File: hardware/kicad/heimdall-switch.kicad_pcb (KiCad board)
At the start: 2 copper layers, 53 x 23 mm, 42 parts, among them J1 SWD (ARM 10-pin), J2 LOAD_OUT, J3 BATT_IN, J4 B3B-XH-A, Q1 AO3400A, Q2 BSS84, Q3 AO4407A, Q4 AO4407A, Q5 AO3400A, Q6 BSS84, SW1 PTS810, U1 BT832, U2 TPS629206, Y1 32.768kHz

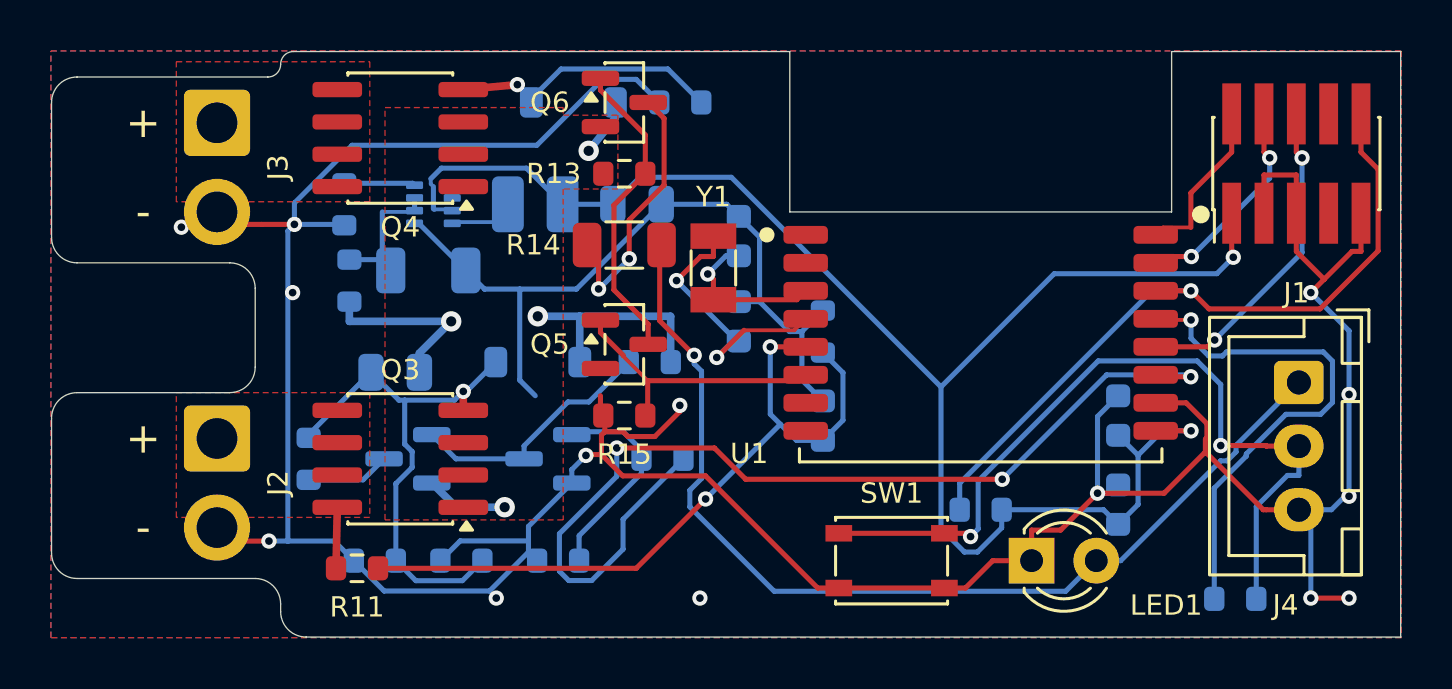
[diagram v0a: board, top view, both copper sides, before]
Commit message: Main PCB: BAT/OUT on silk instead of the J3/J2 references
The labels sit right of each wire pair, outside the heat shrink. The
J3/J2 references move to the fab layer.

Co-Authored-By: Claude Opus 5.5 <noreply@anthropic.com>
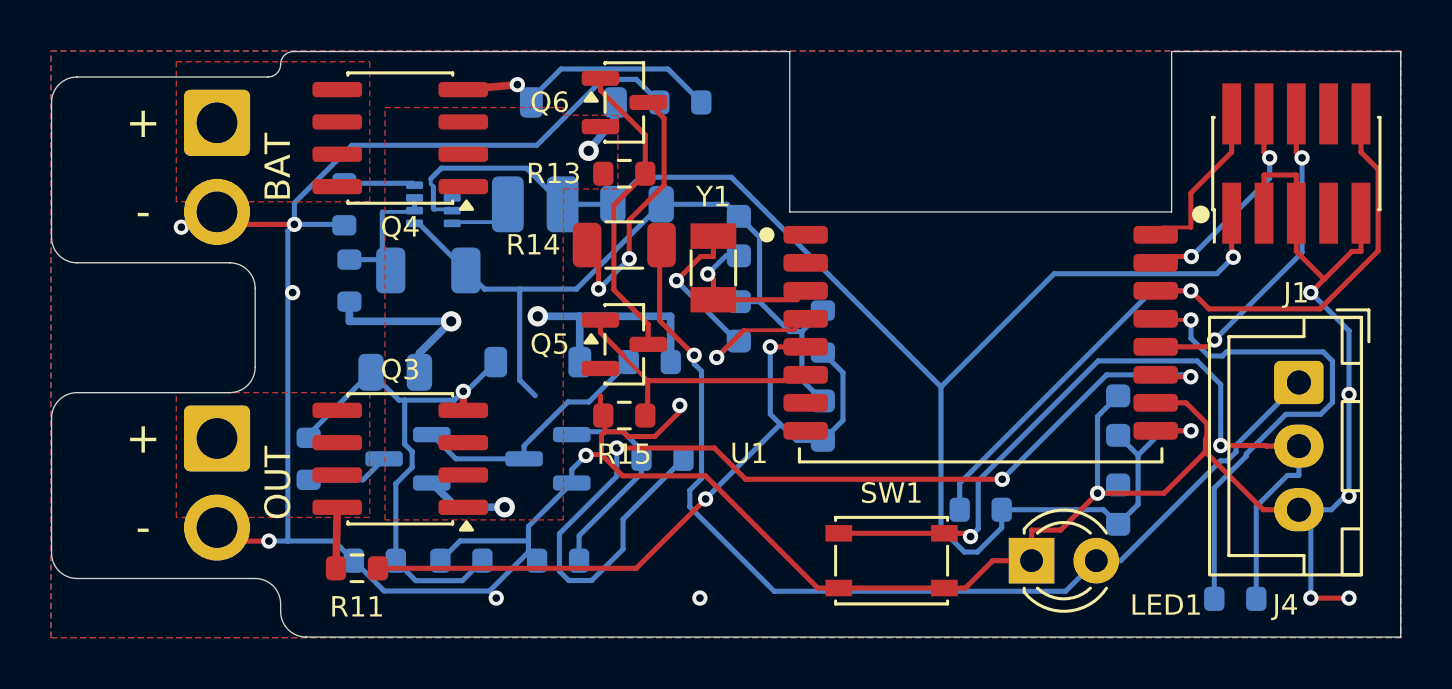
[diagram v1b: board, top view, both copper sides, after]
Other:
- board text added: "BAT"
- board text added: "OUT"
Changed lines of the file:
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@@
 		(tags "connector wire 0.75sqmm")
 		(property "Reference" "J3"
-			(at 1.75 -2.4 90)
-			(layer "F.SilkS")
+			(at 1.75 0 0)
+			(layer "F.Fab")
 			(effects
 				(font
@@
 		(tags "connector wire 0.75sqmm")
 		(property "Reference" "J2"
-			(at 1.75 -2.4 90)
-			(layer "F.SilkS")
+			(at 1.75 0 0)
+			(layer "F.Fab")
 			(effects
 				(font
@@
 		(layer "Edge.Cuts")
 	)
+	(gr_text "BAT"
+		(at 104.9 104.55 90)
+		(layer "F.SilkS")
+		(effects
+			(font
+				(size 1 1)
+				(thickness 0.15)
+			)
+		)
+	)
+	(gr_text "OUT"
+		(at 104.9 116.95 90)
+		(layer "F.SilkS")
+		(effects
+			(font
+				(size 1 1)
+				(thickness 0.15)
+			)
+		)
+	)
 	(gr_text "+"

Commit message: Main PCB: solid B.Cu GND strap for the load return
The OUT- to BAT- return had to squeeze past R8 around the slot end
(~1mm of B.Cu). Now a no-tracks rule area keeps a GND strap free:
3.5mm on B past OUT+, >=2.4mm on B plus ~4.3mm F.Cu beside the slot
end, with a 6-via block where the F copper hands down to the strap.
R8 moved below Q2, R9/R10 shifted down; re-routed, U2-EN finished by
hand. 49 vias, ~570mm. DRC clean, full parity.

Co-Authored-By: Claude Opus 5.5 <noreply@anthropic.com>
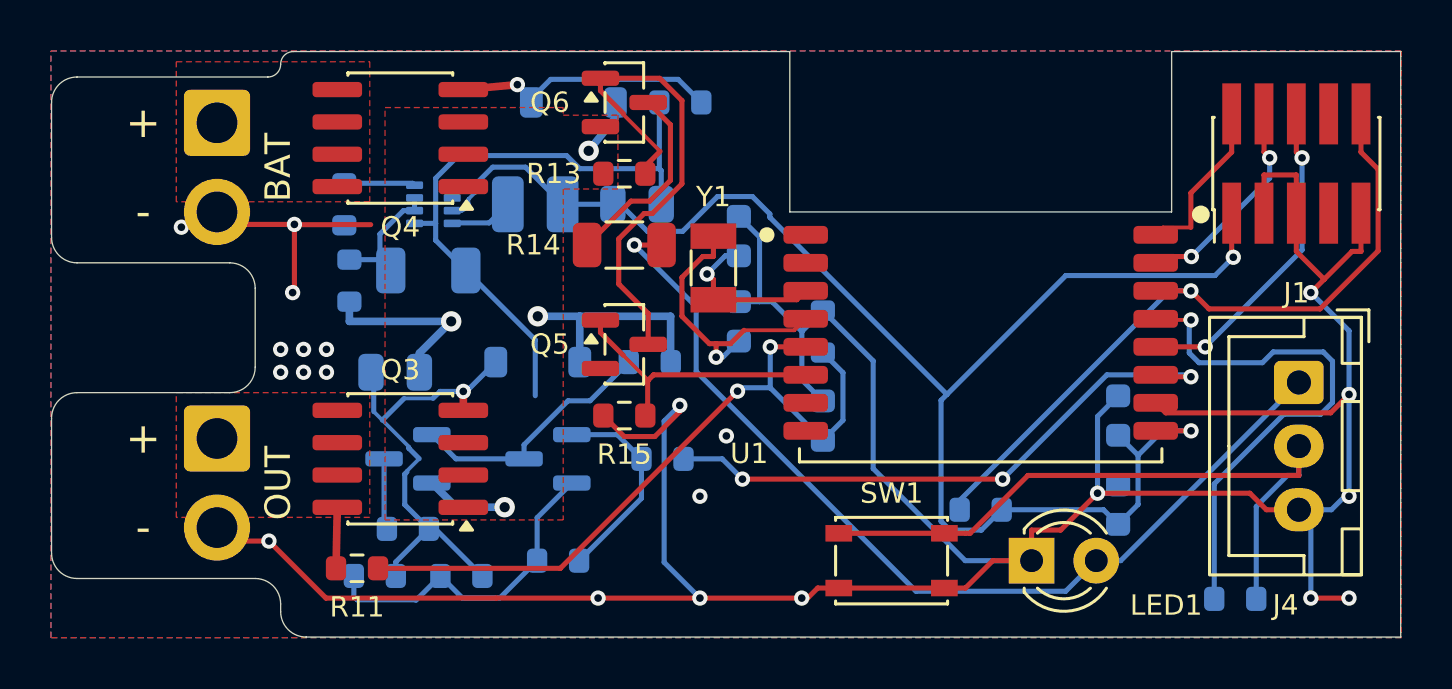
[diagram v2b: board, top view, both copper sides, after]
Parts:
- moved R8 4.77 mm to (110.0, 118.8), turned to 0 degrees
- moved R10 0.60 mm to (112.1, 120.6)
- moved R9 0.60 mm to (108.7, 120.6)
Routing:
- net /OUT_OFF: track 39.7 -> 23.4 mm
- net Net-(Q5-D): track 12.2 -> 19.8 mm
- net GND: track 164.9 -> 171.3 mm, vias 14 -> 22
- net Net-(J4-Pin_2): track 31.8 -> 27.1 mm, vias 2 -> 0
- net +3V3: track 64.3 -> 61.4 mm
- net Net-(Q6-D): track 10.6 -> 7.75 mm, vias 2 -> 0
- net /LED_A: track 40.0 -> 37.7 mm
- net /Q3_GATE: track 21.1 -> 19.0 mm
- net /BTN: track 20.3 -> 21.0 mm
- net Net-(Q2-D): track 3.30 -> 2.80 mm
- net Net-(U1-P0.01_XL2): track 11.2 -> 11.3 mm, vias 2 -> 1

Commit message: Main PCB: tidy GND vias at the wire pads
BAT- island: the scattered vias become a 2 x 5 grid (1.2mm pitch, ~10A
layer transfer). Dropped the redundant via beside the BAT- pad on the
tab, the leftover via and stub at OUT-, and the autorouter's GND stubs
into both pads (the plated pads join the pours directly). DRC clean.

Co-Authored-By: Claude Opus 5.5 <noreply@anthropic.com>
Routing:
- net GND: track 171.3 -> 157.0 mm
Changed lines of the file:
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@@
-	)
-	(segment
-		(start 105.47 109.47)
-		(end 105.54 109.4)
-		(width 0.2)
-		(layer "F.Cu")
-		(net "GND")
 	)
 	(segment
@@
 	)
 	(segment
-		(start 104.54 119.23)
-		(end 106.78 121.47)
-		(width 0.2)
-		(layer "F.Cu")
-		(net "GND")
-	)
-	(segment
-		(start 104.54 119.23)
-		(end 103.03 119.23)
-		(width 0.2)
-		(layer "F.Cu")
-		(net "GND")
-	)
-	(segment
 		(start 145.47 109.47)
 		(end 145.9942 108.9458)
@@
 	)
 	(segment
-		(start 108.5379 106.7995)
-		(end 105.5495 106.7995)
-		(width 0.2)
-		(layer "F.Cu")
-		(net "GND")
-	)
-	(segment
 		(start 131.075 121.075)
 		(end 131.9017 121.075)
@@
 	)
 	(segment
-		(start 105.54 109.4)
-		(end 105.54 106.79)
-		(width 0.2)
-		(layer "F.Cu")
-		(net "GND")
-	)
-	(segment
 		(start 131.075 121.075)
 		(end 126.925 121.075)
@@
 	)
 	(segment
-		(start 103.03 119.23)
-		(end 102.5 118.7)
-		(width 0.2)
-		(layer "F.Cu")
-		(net "GND")
-	)
-	(segment
 		(start 118.4988 115.1238)
 		(end 117.675 114.3)
@@
 	)
 	(segment
-		(start 102.99 106.79)
-		(end 102.5 106.3)
-		(width 0.2)
-		(layer "F.Cu")
-		(net "GND")
-	)
-	(segment
 		(start 125.7033 121.47)
 		(end 126.0983 121.075)
@@
 	)
 	(segment
-		(start 105.54 106.79)
-		(end 102.99 106.79)
-		(width 0.2)
-		(layer "F.Cu")
-		(net "GND")
-	)
-	(segment
 		(start 106.78 121.47)
 		(end 113.47 121.47)
@@
 		(net "GND")
 	)
-	(segment
-		(start 105.5495 106.7995)
-		(end 105.54 106.79)
-		(width 0.2)
-		(layer "F.Cu")
+	(via
+		(at 105.1 111.8)
+		(size 0.6)
+		(drill 0.3)
+		(layers "F.Cu" "B.Cu")
+		(locked yes)
 		(net "GND")
 	)
@@
 	)
 	(via
+		(at 106.3 111.8)
+		(size 0.6)
+		(drill 0.3)
+		(layers "F.Cu" "B.Cu")
+		(locked yes)
+		(net "GND")
+	)
+	(via
 		(at 120.68 113.9)
 		(size 0.6)
@@
 	)
 	(via
+		(at 106.3 110.6)
+		(size 0.6)
+		(drill 0.3)
+		(layers "F.Cu" "B.Cu")
+		(locked yes)
+		(net "GND")
+	)
+	(via
 		(at 121.47 121.47)
 		(size 0.6)
@@
 	)
 	(via
-		(at 106.8 112.6)
+		(at 105.1 109.4)
+		(size 0.6)
+		(drill 0.3)
+		(layers "F.Cu" "B.Cu")
+		(locked yes)
+		(net "GND")
+	)
+	(via
+		(at 105.1 107)
 		(size 0.6)
 		(drill 0.3)
@@
 	)
 	(via
-		(at 105 112.6)
-		(size 0.6)
-		(drill 0.3)
-		(layers "F.Cu" "B.Cu")
-		(locked yes)
-		(net "GND")
-	)
-	(via
 		(at 121.47 117.47)
 		(size 0.6)
@@
 	)
 	(via
-		(at 105 111.7)
-		(size 0.6)
-		(drill 0.3)
-		(layers "F.Cu" "B.Cu")
-		(locked yes)
-		(net "GND")
-	)
-	(via
 		(at 122.51 115.1)
 		(size 0.6)
@@
 	)
 	(via
-		(at 105.9 111.7)
-		(size 0.6)
-		(drill 0.3)
-		(layers "F.Cu" "B.Cu")
-		(locked yes)
-		(net "GND")
-	)
-	(via
-		(at 105.54 106.79)
+		(at 105.1 110.6)
+		(size 0.6)
+		(drill 0.3)
+		(layers "F.Cu" "B.Cu")
+		(locked yes)
+		(net "GND")
+	)
+	(via
+		(at 106.3 108.2)
+		(size 0.6)
+		(drill 0.3)
+		(layers "F.Cu" "B.Cu")
+		(locked yes)
+		(net "GND")
+	)
+	(via
+		(at 106.3 107)
 		(size 0.6)
 		(drill 0.3)
@@
 	)
 	(via
-		(at 101.1 106.9)
-		(size 0.6)
-		(drill 0.3)
-		(layers "F.Cu" "B.Cu")
-		(locked yes)
-		(net "GND")
-	)
-	(via
-		(at 104.54 119.23)
-		(size 0.6)
-		(drill 0.3)
-		(layers "F.Cu" "B.Cu")
-		(locked yes)
-		(net "GND")
-	)
-	(via
 		(at 117.47 121.47)
 		(size 0.6)
@@
 	)
 	(via
-		(at 105.47 109.47)
+		(at 105.1 108.2)
 		(size 0.6)
 		(drill 0.3)
@@
 	)
 	(via
-		(at 106.8 111.7)
-		(size 0.6)
-		(drill 0.3)
-		(layers "F.Cu" "B.Cu")
-		(locked yes)
-		(net "GND")
-	)
-	(via
 		(at 146.97 117.47)
 		(size 0.6)
@@
 	)
 	(via
-		(at 105.9 112.6)
-		(size 0.6)
-		(drill 0.3)
+		(at 106.3 109.4)
+		(size 0.6)
+		(drill 0.3)

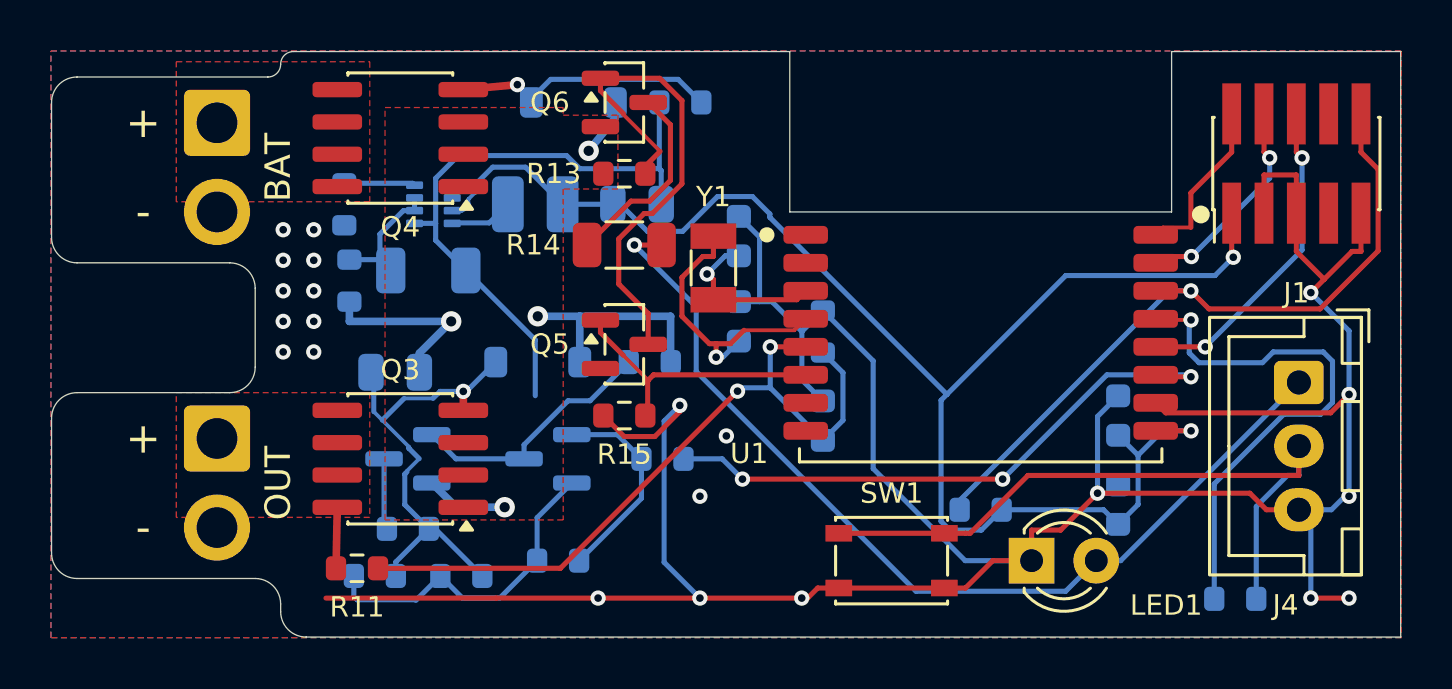
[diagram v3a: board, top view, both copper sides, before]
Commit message: Main PCB: clean-up for JLCDFM
From the JLCDFM report on the first upload:
- vias 0.6/0.3 -> 0.7/0.3 (0.2mm annular ring); the eight that had no
  room were nudged <=0.16mm, one by shifting two neighbouring diagonals
- solder mask expansion 0.05mm (0.025mm on U2, 0.15mm webs) for the
  rounded-pad 'negative expansion' warnings
- XL1/XL2 enter U1 pads 3/4 straight on the centre line (XL2 ran 0.02mm
  under pad 4's mask opening)
- silkscreen: all strokes >=0.15mm, footprint lines clipped >=0.15mm
  from pad openings and holes, labels 1.0mm/0.15mm placed clear of
  vias and the outline (silk_labels.py updated)
- C5 moved from 0.22mm beside LED1's lead (bottom side, a solder-bridge
  risk) to right under U1's VDD pin
- keeps the Gerber plot settings saved from the GUI
'THT to SMD' remains: an assembly-service rule, not relevant for bare
boards. ERC/DRC clean, full parity.

Co-Authored-By: Claude Opus 5.5 <noreply@anthropic.com>
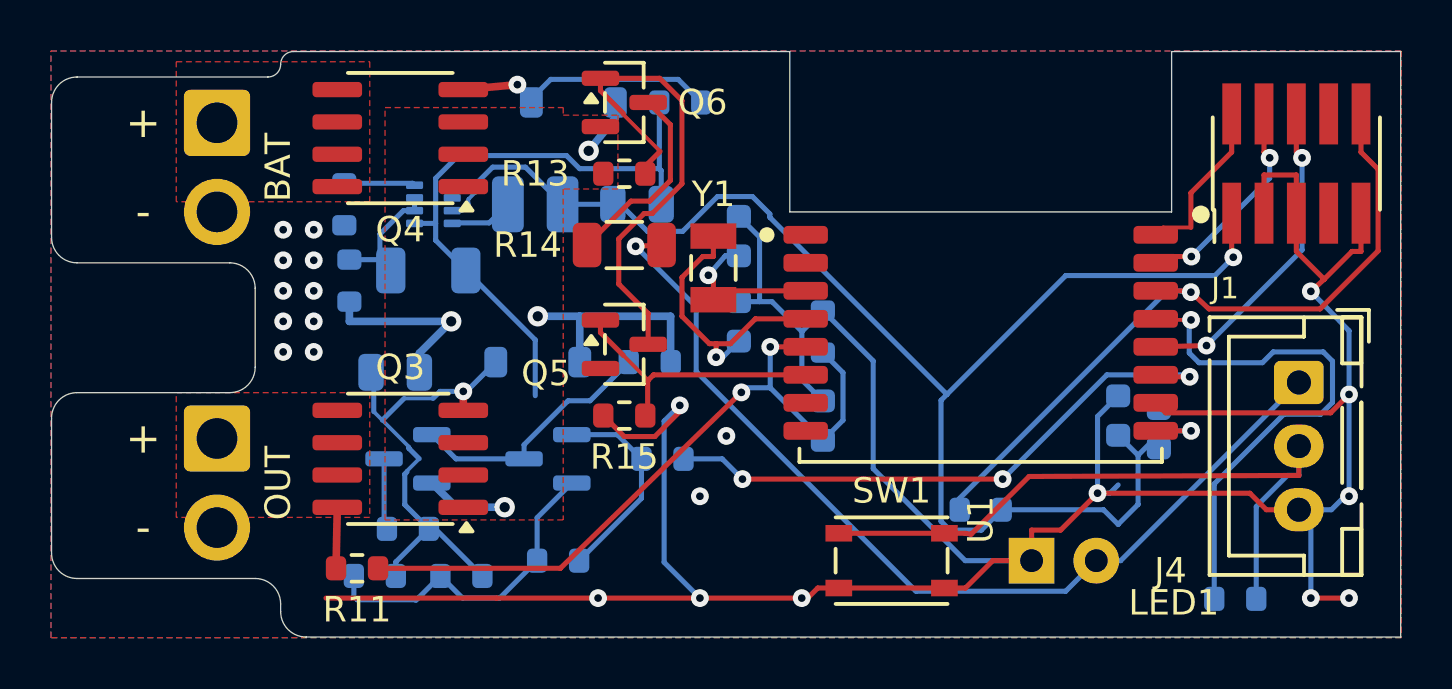
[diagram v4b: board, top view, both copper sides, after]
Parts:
- moved C5 3.40 mm to (139.5, 114.8)
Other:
- rule pad_to_mask_clearance: 0 -> 0.05
